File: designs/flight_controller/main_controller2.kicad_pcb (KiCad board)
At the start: 4 copper layers, 55.1 x 55.1 mm, 73 parts, among them J1 xt30, J10 Conn_01x15, J3 xt30, J4 Conn_01x02, J6 Conn_01x02, J7 Conn_01x02, J8 Conn_01x02, J9 Conn_01x16, Q1 FDN359BN, SW1 SW_SPST, SW2 SW_SPST, U1 ESP32-PICO-D4, U10 BTN7030-1EPA, U11 PCA9557PW, U12 INA219AxD, U13 W25N02KVZEIR, U14 MCP2517FD-xSL, U15 SN65HVD230, U2 BMI088, U3 china_buck_converter, U4 AP7361-33ER-13, U5 MS5611-01BA, U6 BTS70802, U7 BTN7030-1EPA, U8 BTN7030-1EPA, U9 BTN7030-1EPA, Y1 40MHz

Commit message: preliminary layout
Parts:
- removed R2: 2k2, Resistor_SMD:R_0603_1608Metric
- added C20: 4.7u, Capacitor_SMD:C_0603_1608Metric, F.Cu at (228.9, 121.4)
- added C21: 0.1u, Capacitor_SMD:C_0603_1608Metric, B.Cu at (235.0, 138.7)
- added C22: 0.1u, Capacitor_SMD:C_0603_1608Metric, B.Cu at (209.1, 138.5)
- added J2: Conn_Coaxial, Connector_Coaxial:U.FL_Molex_MCRF_73412-0110_Vertical, F.Cu at (209.9, 117.1)
- C11, C12, C17, C2, C3, C8, C9, D6, D7, R3, R5: moved to B.Cu
- R1: value 10k -> 2.2k
- Y1: value 40MHz -> Crystal_GND24_Small; footprint Oscillator:Oscillator_SMD_SeikoEpson_SG8002CE-4Pin_3.2x2.5mm_HandSoldering -> lib:CX3225SB40000D0FLJCC
- moved D3 209.9 mm to (239.1, 148.9), turned to 0 degrees
- moved D5 198.5 mm to (230.5, 148.9), turned to 0 degrees
- moved SW2 194.1 mm to (240.9, 117.6), turned to 180 degrees
- moved SW1 164.5 mm to (240.9, 111.9), turned to 180 degrees
- moved R10 134.0 mm to (204.0, 125.0), turned to 0 degrees
- moved C15 126.9 mm to (221.5, 139.2), turned to 180 degrees
- moved JP5 124.5 mm to (200.2, 125.0)
- moved D7 122.1 mm to (226.1, 152.2), turned to 180 degrees
- moved C13 120.3 mm to (226.9, 133.4)
- moved C6 103.0 mm to (236.3, 128.3), turned to -90 degrees
- moved C7 98.2 mm to (212.1, 129.6), turned to 180 degrees
- moved R3 93.7 mm to (202.4, 130.6), turned to 180 degrees
- moved R12 87.9 mm to (199.5, 120.7)
- moved D6 85.6 mm to (213.1, 148.9)
- moved R5 83.7 mm to (226.2, 150.1)
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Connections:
- D1 pad 1: +3V3 -> +5V
- D2 pad 1: +3V3 -> +5V
- R1 pad 1: Net-(J1-Pad2) -> Earth
- R1 pad 2: /VBAT_SENSE -> Net-(JP1-Pad2)
- U1 pad 1: Net-(U1-Pad1) -> +3V3
- U1 pad 19: unconnected-(U1-Pad19) -> +3V3
- U1 pad 2: unconnected-(U1-Pad2) -> Net-(U1-Pad2)
- U1 pad 3: Net-(U1-Pad3) -> +3V3
- U1 pad 37: unconnected-(U1-Pad37) -> +3V3
- U1 pad 4: Net-(U1-Pad3) -> +3V3
- U1 pad 43: Net-(U1-Pad1) -> +3V3
- U1 pad 46: Net-(U1-Pad1) -> +3V3
- U1 pad 49: unconnected-(U1-Pad49) -> Earth
- U1 pad 7: /CURR_SENSE -> unconnected-(U1-Pad7)
- U1 pad 8: /VBAT_SENSE -> unconnected-(U1-Pad8)
- U10 pad 6: /PYRO_4_EN -> /PYRO_4
- U11 pad 1: /SCL -> /SCL0
- U11 pad 2: /SDA -> /SDA0
- U2 pad 8: /SCL -> /SCL0
- U2 pad 9: /SDA -> /SDA0
- U5 pad 7: /SDA -> /SDA0
- U5 pad 8: /SCL -> /SCL0
- U7 pad 6: /PYRO_1_EN -> /PYRO_1
- U8 pad 6: /PYRO_3_EN -> /PYRO_3
- U9 pad 6: /PYRO_2_EN -> /PYRO_2
- Y1 pad 2: Net-(C18-Pad1) -> Earth
- Y1 pad 3: (no net) -> Net-(C18-Pad1)
- Y1 pad 4: (no net) -> Earth

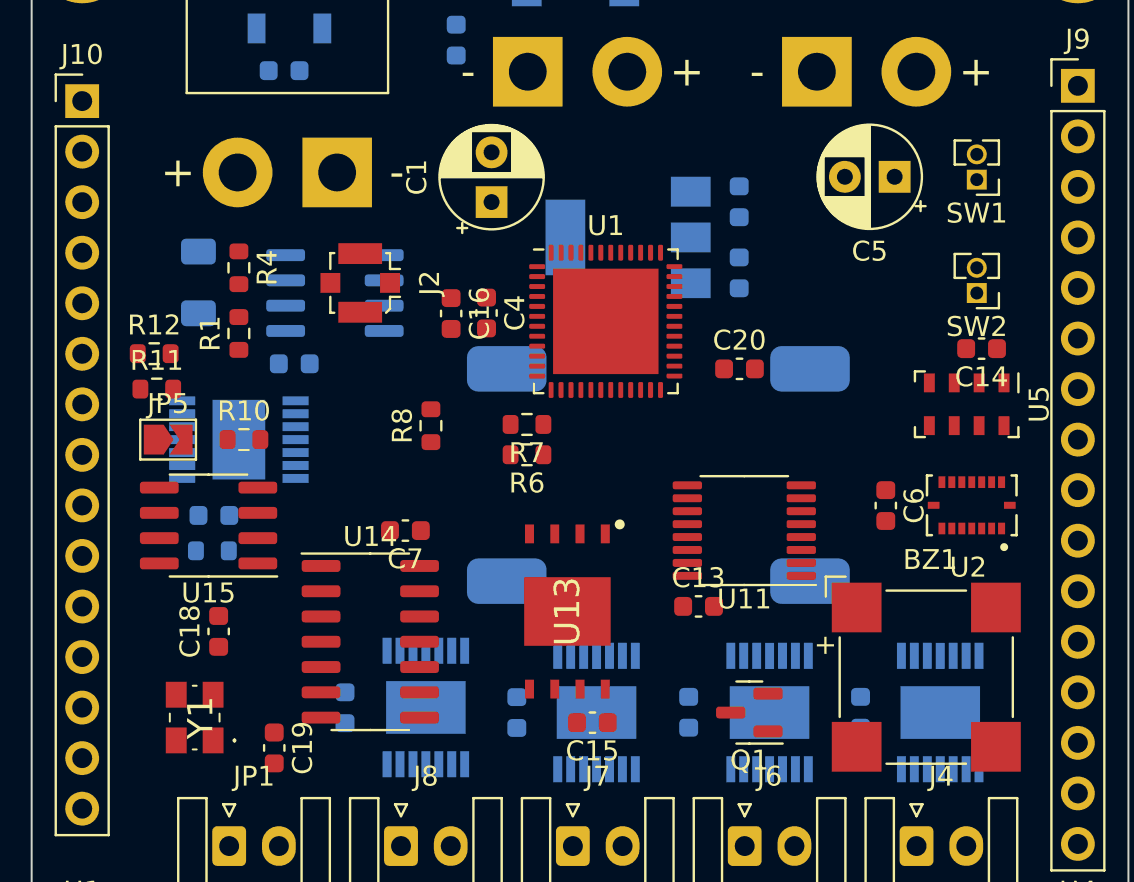
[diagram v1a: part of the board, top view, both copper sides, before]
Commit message: add ufl
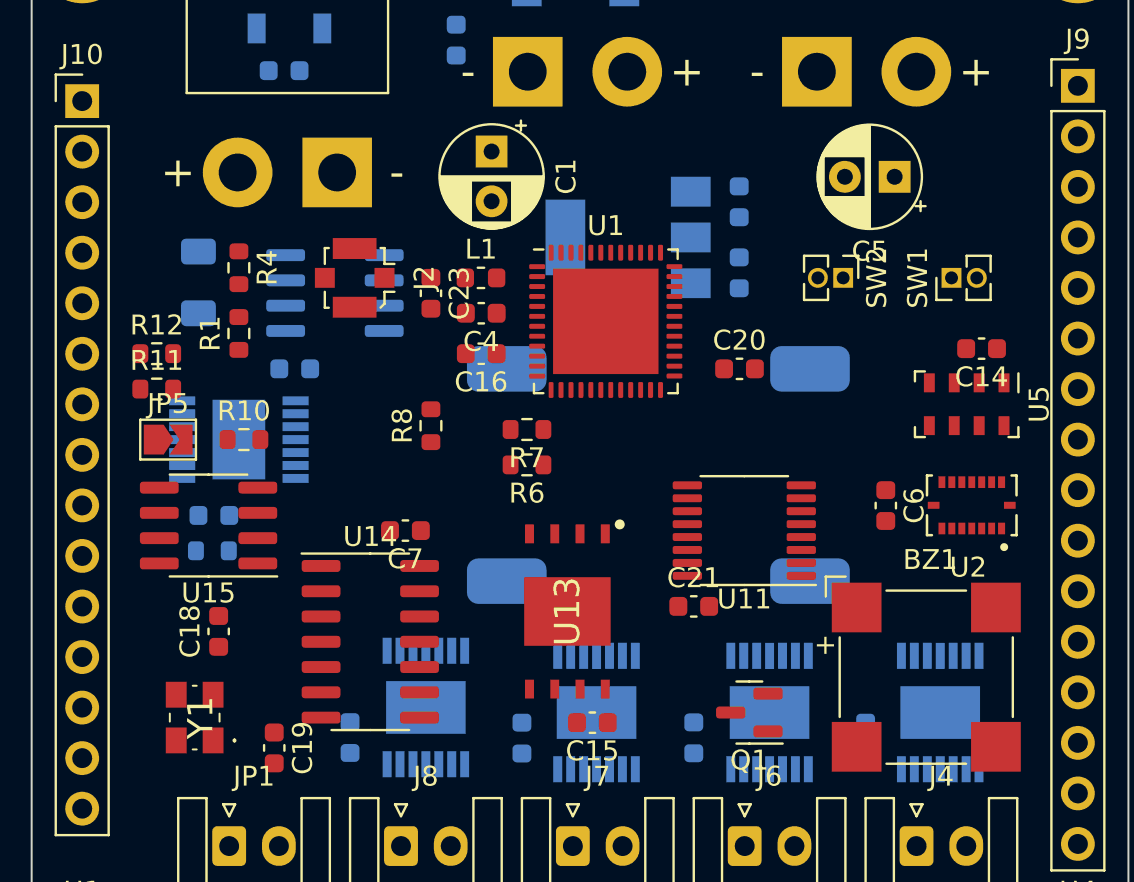
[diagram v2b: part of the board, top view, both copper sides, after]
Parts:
- added C23: tbd, Capacitor_SMD:C_0603_1608Metric, F.Cu at (213.4, 117.6)
- added L1: tbd, Inductor_SMD:L_0603_1608Metric, F.Cu at (215.9, 116.9)
- C13: moved to B.Cu
- C21: moved to F.Cu
- moved C12 19.0 mm to (209.4, 140.0), turned to -90 degrees
- moved C22 17.2 mm to (206.6, 121.4), turned to 0 degrees
- moved C13 10.7 mm to (235.3, 140.0), turned to -90 degrees
- moved C21 9.93 mm to (226.6, 133.4), turned to 0 degrees
- moved SW2 6.76 mm to (234.1, 116.9), turned to -90 degrees
- moved SW1 5.10 mm to (239.6, 116.9), turned to 90 degrees
- moved C1 2.54 mm to (216.5, 110.5), turned to -90 degrees
- moved C16 2.52 mm to (216.0, 120.7), turned to 180 degrees
- moved C11 1.31 mm to (226.6, 140.0)
- moved C10 1.31 mm to (218.0, 140.0)
- moved R6 0.51 mm to (218.3, 126.3)
- moved J2 0.38 mm to (209.6, 116.9)
- moved C4 0.27 mm to (216.0, 118.6), turned to 180 degrees
- moved R7 0.25 mm to (218.3, 124.5)
- moved R12 0.13 mm to (199.6, 120.7)
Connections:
- C10 pad 1: +3V3 -> /EDDA_PWR
- C11 pad 1: +3V3 -> /EDDA_PWR
- C12 pad 1: +3V3 -> /EDDA_PWR
- C13 pad 1: +3V3 -> /EDDA_PWR
- J2 pad 1: Net-(U1-Pad2) -> Net-(J2-Pad1)

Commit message: routing done
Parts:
- added F1: Fuse_Small, Fuse:Fuse_1812_4532Metric_Pad1.30x3.40mm_HandSolder, B.Cu at (208.6, 130.6)
- added R13: 10k, Resistor_SMD:R_0603_1608Metric, F.Cu at (210.6, 121.2)
- added R14: 2k2, Resistor_SMD:R_0603_1608Metric, F.Cu at (210.6, 123.0)
- added R2: 2k2, Resistor_SMD:R_0603_1608Metric, F.Cu at (207.3, 121.2)
- R4: value 2.2k -> 4k7
- Y1: value Crystal_GND24_Small -> CX3225SB40000D0FLJCC
- moved R8 20.6 mm to (233.4, 119.4), turned to 180 degrees
- moved C16 5.08 mm to (216.0, 115.6)
- moved C14 3.28 mm to (237.8, 120.4)
- moved U5 3.28 mm to (237.1, 123.2)
- moved C6 3.08 mm to (238.0, 130.8), turned to 0 degrees
- moved R6 2.90 mm to (216.0, 124.5)
- moved R7 2.90 mm to (216.0, 126.3)
- moved C22 2.32 mm to (208.8, 120.9)
- moved C7 1.55 mm to (213.7, 129.6), turned to 0 degrees
- moved U2 1.30 mm to (239.3, 128.0)
- moved Q1 0.72 mm to (229.9, 138.2), turned to 0 degrees
- moved C20 0.52 mm to (228.4, 121.4)
- moved C21 0.52 mm to (227.2, 133.4)
- moved U10 0.25 mm to (213.2, 138.7)
- moved L1 0.25 mm to (215.9, 117.1)
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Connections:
- D1 pad 2: unconnected-(D1-Pad2) -> Net-(D1-Pad2)
- D1 pad 4: Net-(D1-Pad4) -> /LED_RMT
- D2 pad 2: Net-(D1-Pad4) -> unconnected-(D2-Pad2)
- D2 pad 4: /LED_TX -> Net-(D1-Pad2)
- J10 pad 1: /GND -> Earth
- J10 pad 11: /5V -> +3V3
- J10 pad 12: VCC -> /EDDA_PWR
- J10 pad 13: VCC -> /EDDA_PWR
- J10 pad 14: /GND -> Earth
- J10 pad 15: /GND -> Earth
- J10 pad 2: /GND -> Earth
- J10 pad 3: VCC -> /EDDA_PWR
- J10 pad 4: VCC -> /EDDA_PWR
- J10 pad 5: /3V3 -> +5V
- J9 pad 1: /GND -> Earth
- J9 pad 12: /GND -> Earth
- J9 pad 13: /MISC_GPIO0 -> /MISC_IO0
- J9 pad 14: /MISC_GPIO1 -> /MISC_IO1
- J9 pad 15: /MISC_GPIO2 -> /MISC_IO2
- J9 pad 16: /GND -> Earth
- J9 pad 8: /GND -> Earth
- U1 pad 21: /PYRO_1 -> /PYRO_2_EN
- U1 pad 22: /MISC_IO0 -> /PYRO_1_EN
- U1 pad 24: /MISC_IO0 -> /BUZZER
- U1 pad 35: /PYRO_2 -> /MISC_IO0
- U1 pad 6: /RX1 -> unconnected-(U1-Pad6)
- U1 pad 7: unconnected-(U1-Pad7) -> /RX1
- U1 pad 8: unconnected-(U1-Pad8) -> /SHORT_SENSE
- U10 pad 6: /PYRO_4 -> /PYRO_4_EN
- U11 pad 13: /MISC_IO3 -> unconnected-(U11-Pad13)
- U11 pad 7: /PYRO_3 -> /PYRO_3_EN
- U11 pad 9: /PYRO_4 -> /PYRO_4_EN
- U6 pad 12: /EDDA_PWR -> Net-(U6-Pad12)
- U6 pad 13: /EDDA_PWR -> Net-(U6-Pad12)
- U6 pad 14: /EDDA_PWR -> Net-(U6-Pad12)
- U7 pad 6: /PYRO_1 -> /PYRO_1_EN
- U8 pad 6: /PYRO_3 -> /PYRO_3_EN
- U9 pad 6: /PYRO_2 -> /PYRO_2_EN
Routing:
- net Earth: track 0.00 -> 199.1 mm, vias 0 -> 29
- net +3V3: track 0.00 -> 152.8 mm, vias 0 -> 29
- net +5V: track 0.00 -> 100.6 mm, vias 0 -> 1
- net /EDDA_PWR: track 0.00 -> 86.6 mm, vias 0 -> 6
- net /SDA1: track 0.00 -> 48.9 mm, vias 0 -> 2
- net /PYRO_1_EN: track 0.00 -> 47.1 mm, vias 0 -> 1
- net /VSPI_MISO: track 0.00 -> 46.0 mm, vias 0 -> 1
- net /SCL0: track 0.00 -> 44.3 mm, vias 0 -> 5
- net /SDA0: track 0.00 -> 44.2 mm, vias 0 -> 3
- net /EDDA_EN: track 0.00 -> 42.9 mm, vias 0 -> 2
- net /MISC_IO0: track 0.00 -> 42.6 mm
- net /TX1: track 0.00 -> 40.9 mm, vias 0 -> 1
- net /RX1: track 0.00 -> 39.8 mm, vias 0 -> 1
- net Net-(JP1-Pad2): track 0.00 -> 39.5 mm, vias 0 -> 2
- net /MISC_IO1: track 0.00 -> 36.5 mm, vias 0 -> 1
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- added copper zone on In2.Cu, net +3V3
- added copper zone on In2.Cu, net /EDDA_PWR
- added copper zone on In1.Cu, net Earth

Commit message: final design
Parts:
- moved C1 2.54 mm to (216.5, 113.1), turned to 90 degrees
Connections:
- C1 pad 1: Earth -> VCC
- C1 pad 2: VCC -> Earth
- U15 pad 5: +3V3 -> unconnected-(U15-Pad5)
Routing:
- net +3V3: track 152.8 -> 149.9 mm, vias 29 -> 30
